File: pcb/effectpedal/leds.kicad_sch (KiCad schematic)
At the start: 81 parts

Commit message: Made progress on the PCB
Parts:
- removed TP? (x16): TestPoint, symbol Connector:TestPoint
- added C17, C18: 0.1u, Capacitor_SMD:C_0805_2012Metric, symbol Device:C_Small
- added J19, J20: Conn_01x04_Male, Connector_PinHeader_2.54mm:PinHeader_1x04_P2.54mm_Vertical, symbol Connector:Conn_01x04_Male
- D17, D18, D19, D20, D21, D22, D23, D24, D25, D26, D27, D28, D29, D30, D31, D32, D33, D34, D35, D36, D37, D38, D39, D40, D41, D42, D43, D44, D45, D46, D47, D48, D49, D50, D51, D52, D53, D54, D55, D56, D57, D58, D59, D60, D61, D62, D63, D64, D65, D66, D67, D68, D69, D70, D71, D72, D73, D74, D75, D76, D77, D78, D79, D80: renamed from D?; footprint (none) -> LED_SMD:LED_0805_2012Metric
- IC5: renamed from IC?; footprint QFN50P400X400X80-25N-D -> footprints:QFN50P400X400X80-25N-D
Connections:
- net LED_SDA: now reaches IC5.1 (SDA)
- net LED_SDA: now also J20.3 (Pin_3)
- net LED_3V3: now reaches IC5.11 (VCC)
- net LED_3V3: now also C17.1, J20.2 (Pin_2)
- net LED_SCL: now reaches IC5.2 (SCL)
- net LED_SCL: now also J20.4 (Pin_4)
- net GND2: now reaches IC5.20 (GND_1)
- net GND2: now also IC5.25 (GND_2), IC5.6 (AD), C17.2, C18.2, J19.1 (Pin_1), J19.2 (Pin_2), J19.3 (Pin_3), J20.1 (Pin_1)
- net LED_RST: now reaches IC5.4 (IN)
- net LED_RST: now also J19.4 (Pin_4)
- net at IC5.5 (C_FILT): now also C18.1
- no-connect marks 0 -> 1
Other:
- note added: "LED Matrix"
- note added: "Left side connector"
- note added: "Right side connector"
- company: (none) -> Anton Liakhovitch
- title: (none) -> CRONCH LED Board
- moved on the sheet: D17, D18, D19, D20, D21, D22, D23, D24, D25, D26, D27, D28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

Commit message: Mostly finished PCB
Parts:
- C17, C18: Digikey Part Number (none) -> 478-1395-2-ND; Digikey Price/Stock (none) -> https://www.digikey.com/en/products/detail/kyocera-avx/0805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; MANUFACTURER (none) -> KYOCERA AVX; MPN (none) -> 08055C104KAT2A; Manufacturer_Name (none) -> KYOCERA AVX; Manufacturer_Part_Number (none) -> 08055C104KAT2A
- D17, D18, D19, D20, D21, D22, D23, D24, D25, D26, D27, D28, D29, D30, D31, D32, D33, D34, D35, D36, D37, D38, D39, D40, D41, D42, D43, D44, D45, D46, D47, D48: value LED -> LED, red; Digikey Part Number (none) -> 732-4984-2-ND; Digikey Price/Stock (none) -> https://www.digikey.com/en/products/detail/w%C3%BCrth-elekt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; MANUFACTURER (none) -> Würth Elektronik; MPN (none) -> 150080RS75000; Manufacturer_Name (none) -> Würth Elektronik; Manufacturer_Part_Number (none) -> 150080RS75000
- D49, D50, D51, D52, D53, D54, D55, D56, D57, D58, D59, D60, D61, D62, D63, D64, D65, D66, D67, D68, D69, D70, D71, D72, D73, D74, D75, D76, D77, D78, D79, D80: value LED -> LED, green; Digikey Part Number (none) -> 732-4983-2-ND; Digikey Price/Stock (none) -> https://www.digikey.com/en/products/detail/w%C3%BCrth-elekt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; MANUFACTURER (none) -> Würth Elektronik; MPN (none) -> 150080GS75000; Manufacturer_Name (none) -> Würth Elektronik; Manufacturer_Part_Number (none) -> 150080GS75000
- IC5: Digikey Part Number (none) -> 2521-IS31FL3728-QFLS2-TR-ND; Digikey Price/Stock (none) -> https://www.digikey.com/en/products/detail/lumissil-microsy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; MANUFACTURER (none) -> Integrated Silicon Solution Inc.; MPN (none) -> IS31FL3728-QFLS2-TR

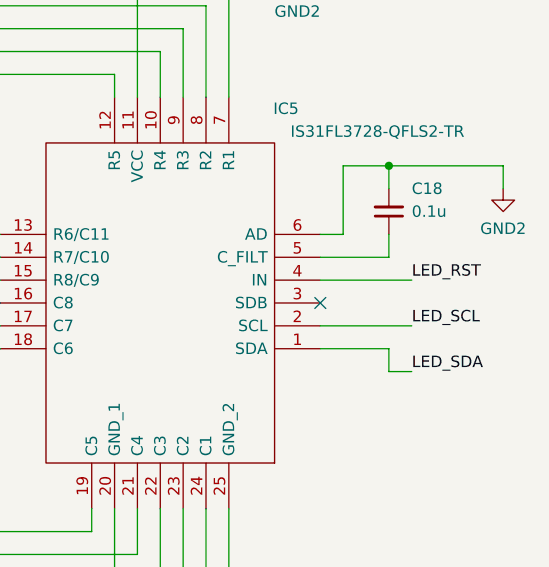
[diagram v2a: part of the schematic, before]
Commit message: Added more test code and deleted some useless stuff
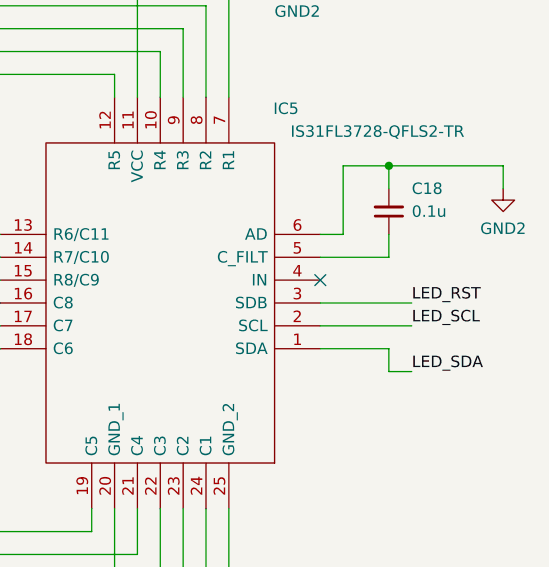
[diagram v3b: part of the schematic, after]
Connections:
- net LED_RST: now also IC5.3 (SDB); no longer IC5.4 (IN)
